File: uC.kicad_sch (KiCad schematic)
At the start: 3 parts, among them J2 OLED

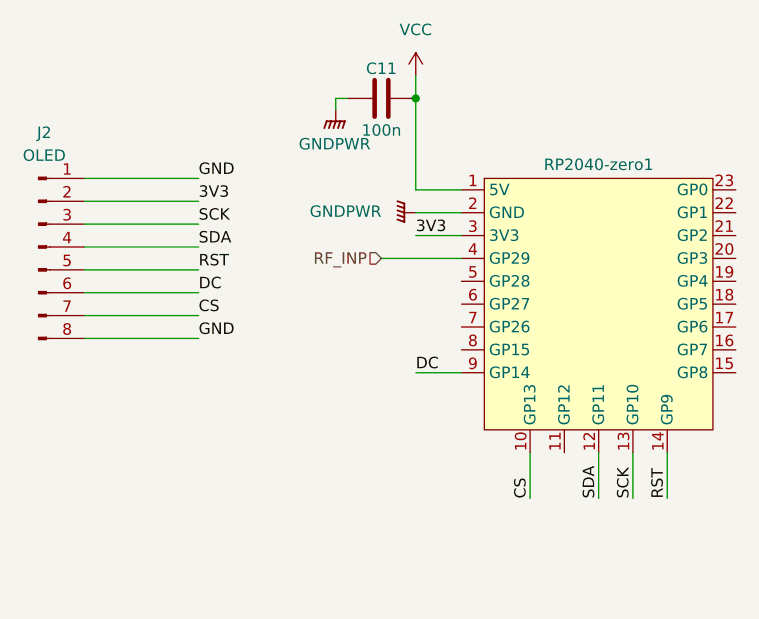
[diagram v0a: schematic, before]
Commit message: dodane C10
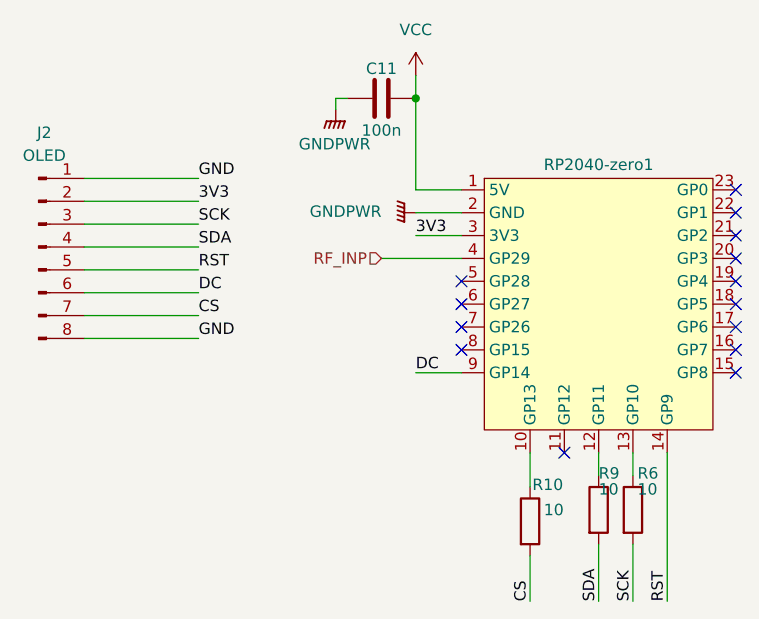
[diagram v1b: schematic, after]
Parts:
- added R10, R6, R9: 10, Resistor_SMD:R_1206_3216Metric_Pad1.30x1.75mm_HandSolder, symbol Device:R
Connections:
- net CS: now also R10.2; no longer RP2040-zero1.10 (GP13)
- net SCK: now also R6.2; no longer RP2040-zero1.13 (GP10)
- net SDA: now also R9.2; no longer RP2040-zero1.12 (GP11)
- new net: R9.1, RP2040-zero1.12 (GP11)
- new net: R10.1, RP2040-zero1.10 (GP13)
- new net: R6.1, RP2040-zero1.13 (GP10)
- no-connect marks 0 -> 14

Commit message: test111
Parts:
- renumbered C11 to C12
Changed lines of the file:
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@@
 		(on_board yes)
 		(dnp no)
-		(property "Reference" "C11"
+		(property "Reference" "C12"
 			(at 86.36 32.258 90)
 			(effects
@@
 			(project ""
 				(path "/6e9b0ecb-5ff8-4cea-bb01-e8c92e636c95/47922e9f-8839-4dfe-b2ac-5d132f76ea44"
-					(reference "C11")
+					(reference "C12")
 					(unit 1)
 				)

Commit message: ostatnie zmiany 09.08.2024
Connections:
- net GND is gone; now on net GNDPWR: J2.1 (Pin_1), J2.8 (Pin_8)
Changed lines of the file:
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@@
 		(color 0 0 0 0)
 	)
+	(junction
+		(at 62.23 62.23)
+		(diameter 0)
+		(color 0 0 0 0)
+	)
 	(no_connect
 		(at 125.73 58.42)
@@
 	(wire
 		(pts
-			(xy 53.34 62.23) (xy 66.04 62.23)
+			(xy 53.34 62.23) (xy 62.23 62.23)
 		)
 		(stroke
@@
 	(wire
 		(pts
+			(xy 62.23 62.23) (xy 62.23 68.58)
+		)
+		(stroke
+			(width 0)
+			(type default)
+		)
+	)
+	(wire
+		(pts
 			(xy 102.87 74.93) (xy 102.87 78.74)
 		)
@@
 		(pts
 			(xy 53.34 52.07) (xy 66.04 52.07)
+		)
+		(stroke
+			(width 0)
+			(type default)
+		)
+	)
+	(wire
+		(pts
+			(xy 62.23 62.23) (xy 66.04 62.23)
 		)
 		(stroke
@@
 					(unit 1)
 				)
+			)
+		)
+	)
+	(symbol
+		(lib_id "power:GNDPWR")
+		(at 62.23 68.58 0)
+		(unit 1)
+		(exclude_from_sim no)
+		(in_bom yes)
+		(on_board yes)
+		(dnp no)
+		(fields_autoplaced yes)
+		(property "Reference" "#PWR026"
+			(at 62.23 73.66 0)
+			(effects
+				(font
+					(size 1.27 1.27)
+				)
+				(hide yes)
+			)
+		)
+		(property "Value" "GNDPWR"
+			(at 62.103 72.39 0)
+			(effects
+				(font
+					(size 1.27 1.27)
+				)
+			)
+		)
+		(property "Footprint" ""
+			(at 62.23 69.85 0)
+			(effects
+				(font
+					(size 1.27 1.27)
+				)
+				(hide yes)
+			)
+		)
+		(property "Datasheet" ""
+			(at 62.23 69.85 0)
+			(effects
+				(font
+					(size 1.27 1.27)
+				)
+				(hide yes)
+			)
+		)
+		(property "Description" "Power symbol creates a global label with name \"GNDPWR\" , global ground"
+			(at 62.23 68.58 0)
+			(effects
+				(font
+					(size 1.27 1.27)
+				)
+				(hide yes)
+			)
+		)
+		(pin "1"
+		)
+		(instances
+			(project ""
+				(path "/6e9b0ecb-5ff8-4cea-bb01-e8c92e636c95/47922e9f-8839-4dfe-b2ac-5d132f76ea44"
+					(reference "#PWR026")
+					(unit 1)
+				)

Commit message: usunięte część ostrzeżeń i błędów
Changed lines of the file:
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@@
 	)
 	(symbol
-		(lib_name "RP2040-zero_1")
 		(lib_id "RP2040-zero:RP2040-zero")
 		(at 110.49 71.12 0)
